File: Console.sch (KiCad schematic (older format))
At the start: 20 parts, among them CON1 microUSB-B, U16 AP2120N-1.8TRG1, U17 FT230XS

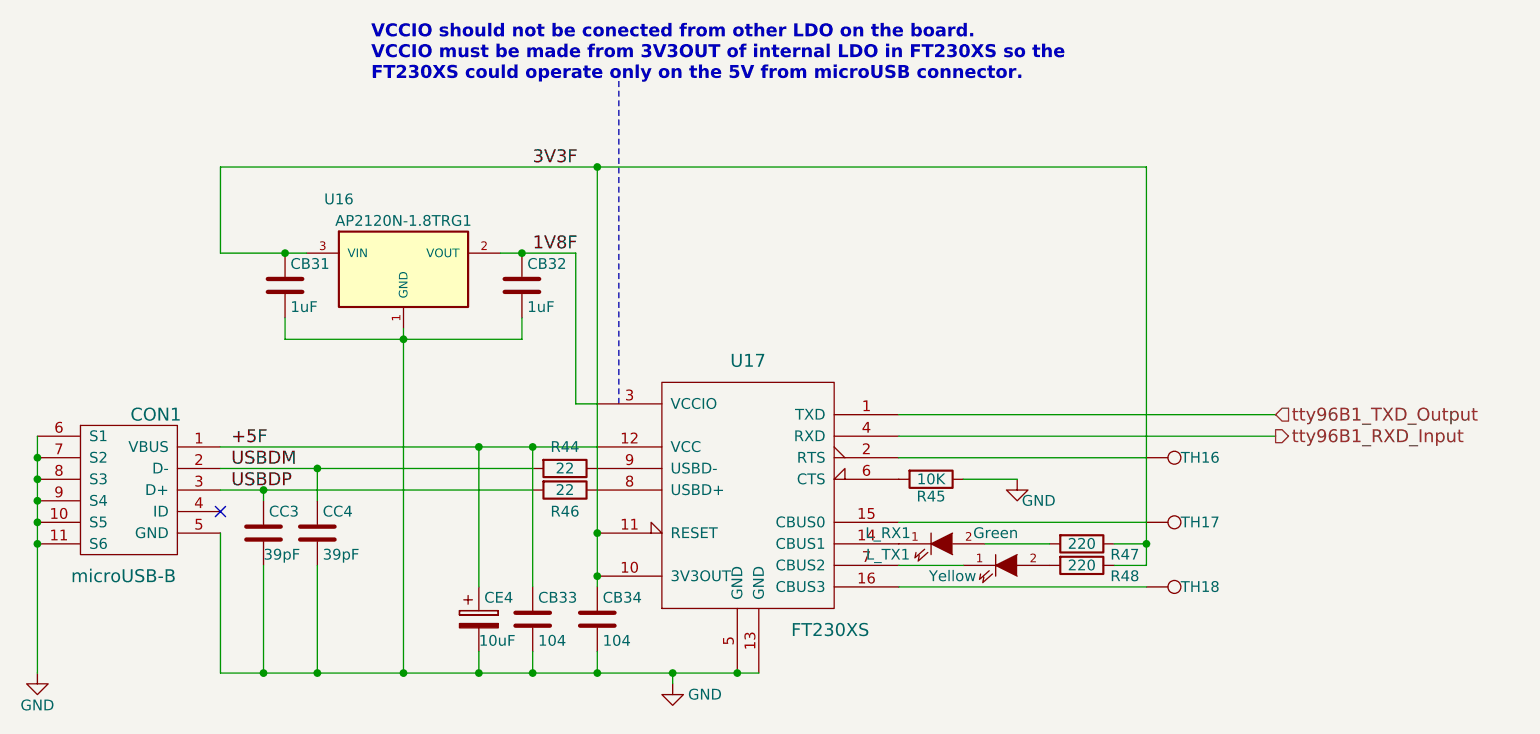
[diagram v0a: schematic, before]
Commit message: Fixed MCP2525 wrong package
Signed-off-by: Akira Tsukamoto <akira-t@s9.dion.ne.jp>
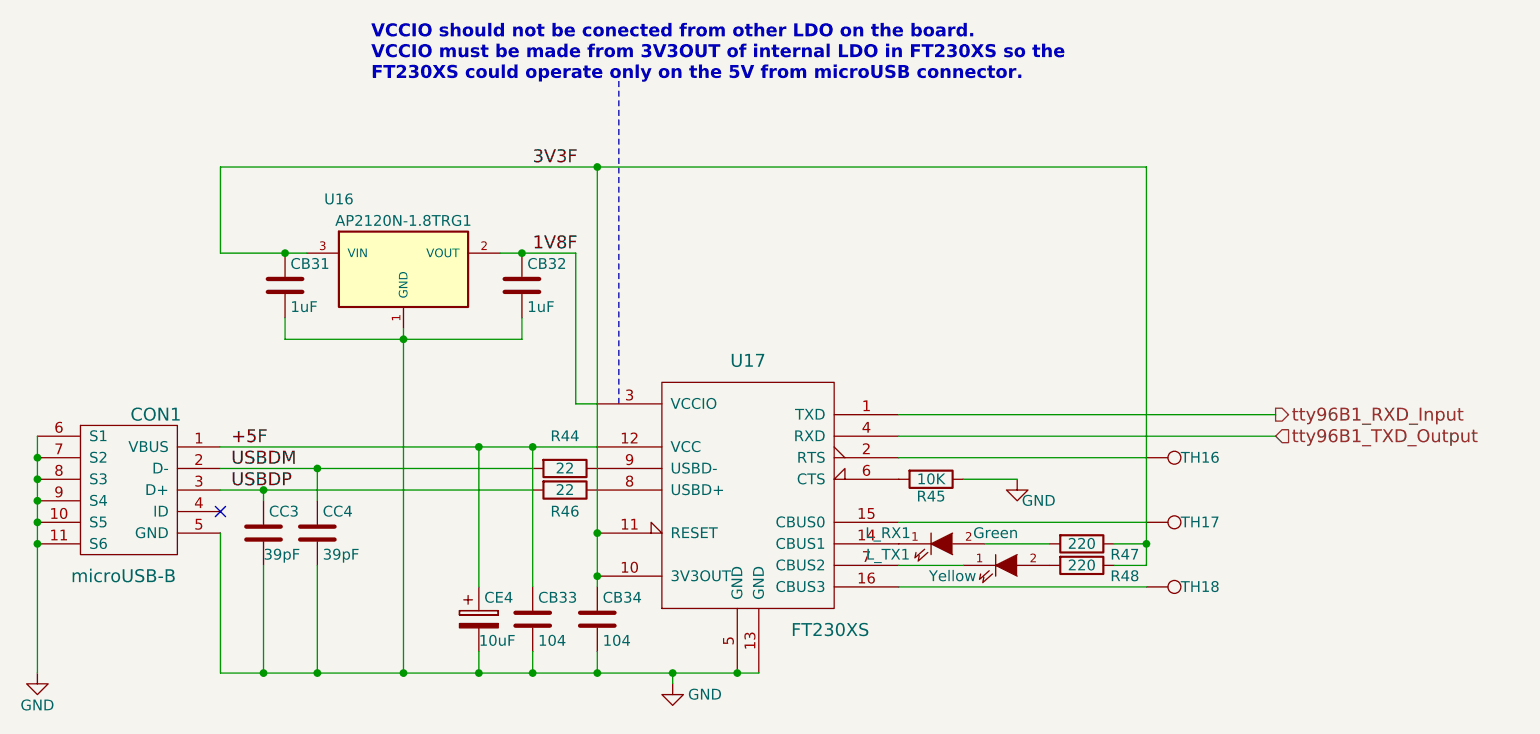
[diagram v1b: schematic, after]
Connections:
- net tty96B1_RXD_Input: now also U17.1 (TXD); no longer U17.4 (RXD)
- net tty96B1_TXD_Output: now also U17.4 (RXD); no longer U17.1 (TXD)
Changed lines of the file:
@@
 Title "DCoJA Yatagarasu Mezzanine"
 Date "2017-03-31"
-Rev "0.10"
+Rev "0.10.1"
 Comp "DroneWorks Inc."
 Comment1 "Copyright (c) 2017 DroneWorks Inc."
@@
 U 1 1 5703FA06
 P 5350 3750
-F 0 "R44" V 5250 3750 50  0000 C CNN
+F 0 "R44" V 5200 3750 50  0000 C CNN
 F 1 "22" V 5350 3750 50  0000 C CNN
 F 2 "droneworks:R_0603_Hand_droneworks" V 5280 3750 30  0001 C CNN
@@
 Wire Wire Line
 	5850 4750 5850 4700
-Text HLabel 8650 3500 2    60   Input ~ 0
+Text HLabel 8650 3600 2    60   Input ~ 0
 tty96B1_TXD_Output
-Text HLabel 8650 3600 2    60   Output ~ 0
+Text HLabel 8650 3500 2    60   Output ~ 0
 tty96B1_RXD_Input
 Connection ~ 4600 4700
